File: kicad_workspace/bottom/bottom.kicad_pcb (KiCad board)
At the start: 2 copper layers, 76.8 x 84 mm, 12 parts, among them M1 N20_MOTOR_EXTENDED_SHAFT, M2 N20_MOTOR_EXTENDED_SHAFT, U1 DRV8833PWP, U2 ULTRASOUND_T_R, U3 ATmega4809-A, U4 BNO055, Y1 32.768kHz

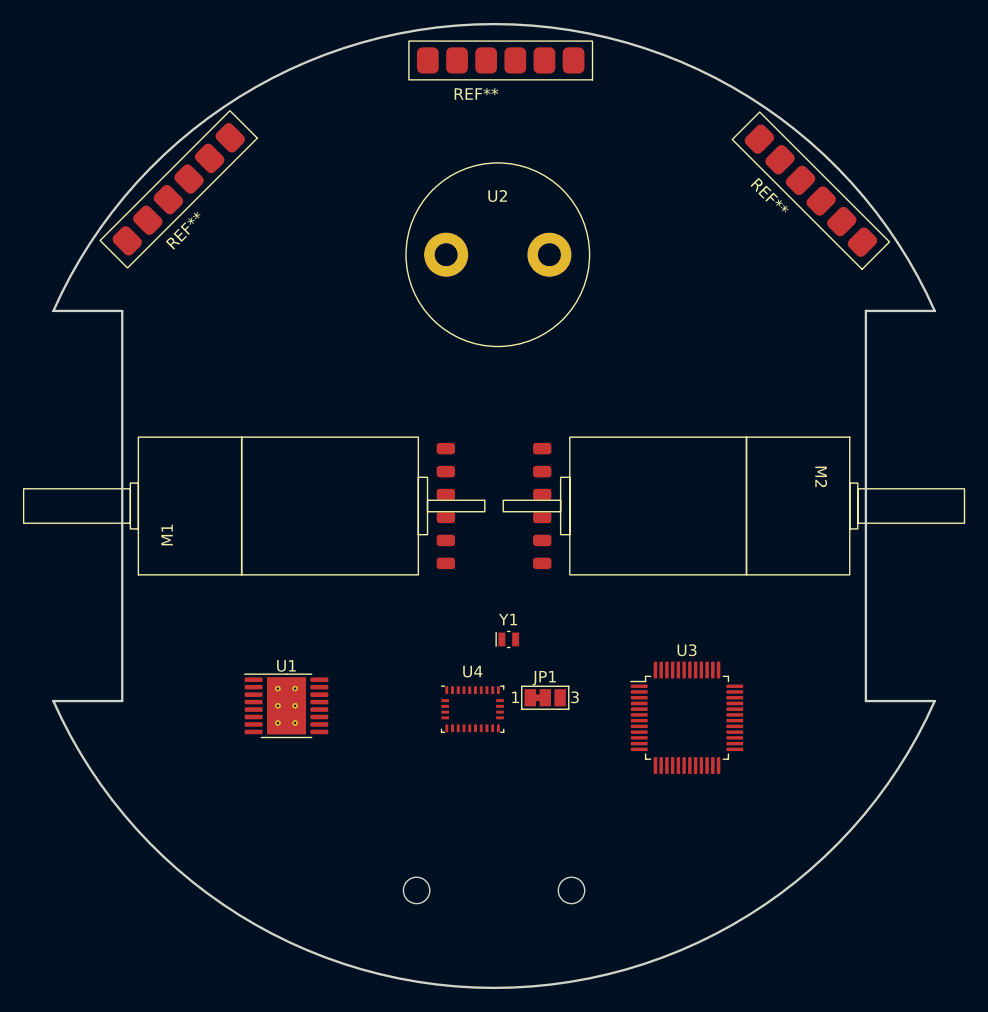
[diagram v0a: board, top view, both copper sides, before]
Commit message: add vl53l0x to schematic, connect footprint to sensors symbol
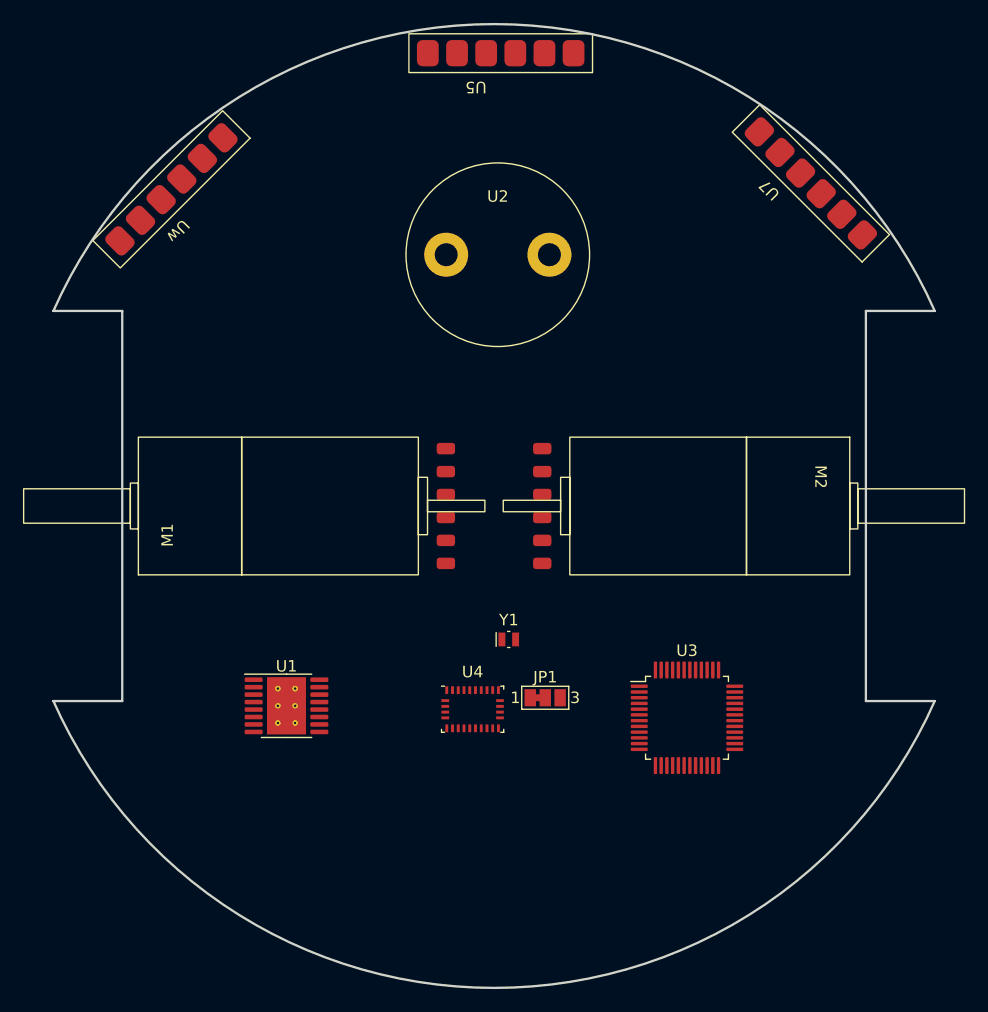
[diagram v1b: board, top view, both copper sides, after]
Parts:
- removed REF** (x3): VL53L0X, pololu:VL53L0X
- removed REF**: BALL_CASTER_3_8, pololu:BALL_CASTER_3_8
- added U5: ~, pololu:VL53L0X, F.Cu at (68.6, 22.2)
- added U7: ~, pololu:VL53L0X, F.Cu at (92.1, 38.7)
- added Uw: ~, pololu:VL53L0X, F.Cu at (38.7, 27.9)
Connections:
- net BNO_SCL renamed SCL
- net BNO_SDA renamed SDA
- U3 pad 10: unconnected-(U3-PC0-Pad10) -> VL_EN1
- U3 pad 11: unconnected-(U3-PC1-Pad11) -> VL_EN2
- U3 pad 12: unconnected-(U3-PC2-Pad12) -> VL_EN3

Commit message: change vcc and vdd symbols. add routes for bno055 sensor on pcb
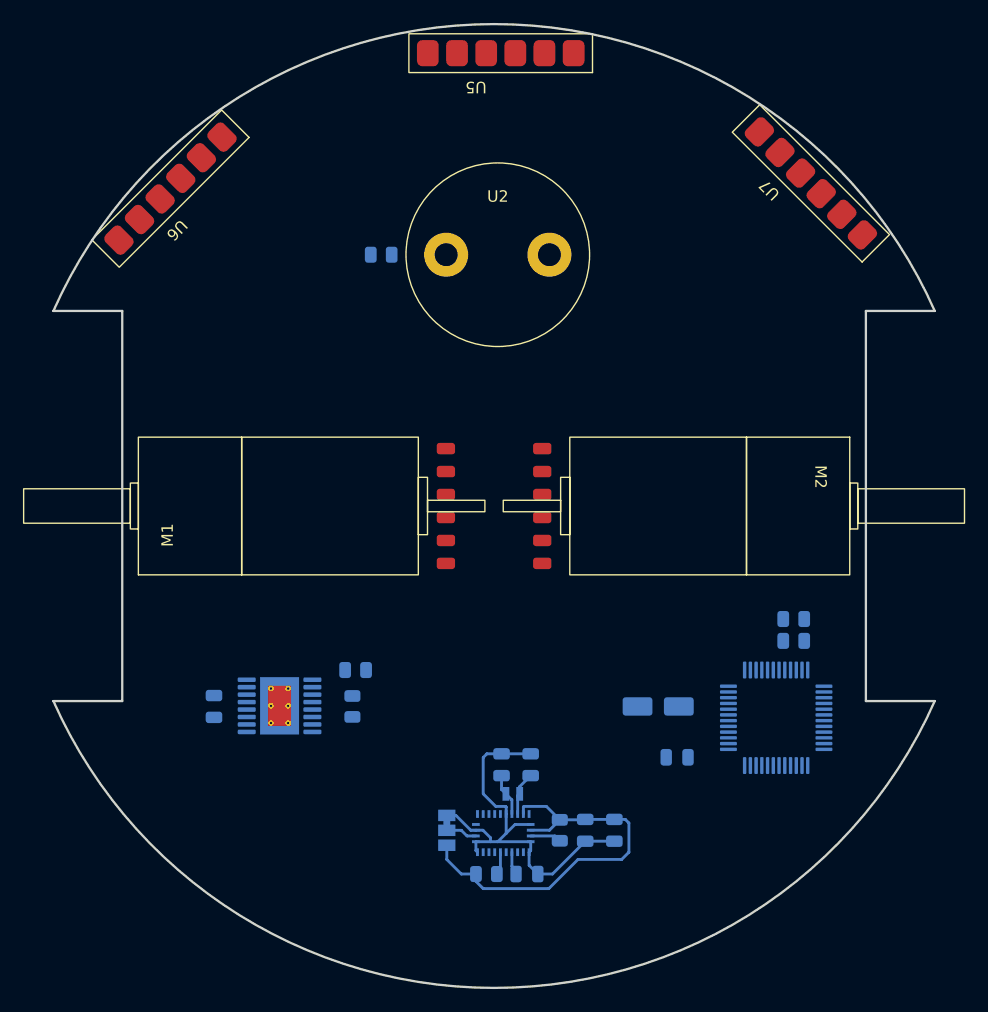
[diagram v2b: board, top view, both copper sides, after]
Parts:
- removed Uw: ~, pololu:VL53L0X
- added C1: 10nF, Capacitor_SMD:C_0805_2012Metric, B.Cu at (35.6, 77.5)
- added C2: 100nF, Capacitor_SMD:C_0805_2012Metric, B.Cu at (76.0, 81.9)
- added C3: 10uF, Capacitor_SMD:CP_Elec_4x3, B.Cu at (74.3, 77.5)
- added C4: 1uF, Capacitor_SMD:C_0805_2012Metric, B.Cu at (62.9, 92.1)
- added C5: 100nF, Capacitor_SMD:C_0805_2012Metric, B.Cu at (70.5, 88.3)
- added C6: 22pF, Capacitor_SMD:C_0805_2012Metric, B.Cu at (60.6, 82.5)
- added C7: 22pF, Capacitor_SMD:C_0805_2012Metric, B.Cu at (63.2, 82.5)
- added C8: 120nF, Capacitor_SMD:C_0805_2012Metric, B.Cu at (67.9, 88.3)
- added R1: 0.2R, Resistor_SMD:R_0805_2012Metric, B.Cu at (47.9, 74.3)
- added R2: 0.2R, Resistor_SMD:R_0805_2012Metric, B.Cu at (47.7, 77.5)
- added R3: R, Resistor_SMD:R_0805_2012Metric, B.Cu at (50.2, 38.1)
- added R4: 10K, Resistor_SMD:R_0805_2012Metric, B.Cu at (59.3, 92.1)
- added R5: 10K, Resistor_SMD:R_0805_2012Metric, B.Cu at (65.7, 88.3)
- added R6: R, Resistor_SMD:R_0805_2012Metric, B.Cu at (86.1, 69.8)
- added R7: R, Resistor_SMD:R_0805_2012Metric, B.Cu at (86.1, 71.8)
- added U6: ~, pololu:VL53L0X, F.Cu at (38.6, 27.9)
- JP1, U1, U3, U4, Y1: moved to B.Cu
- moved JP1 14.4 mm to (55.9, 88.3), turned to -90 degrees
- moved Y1 13.5 mm to (61.6, 85.1), turned to 180 degrees
- moved U4 11.1 mm to (60.8, 88.5), turned to 180 degrees
- moved U3 7.77 mm to (84.6, 78.5), turned to 180 degrees
- moved U1 0.60 mm to (41.3, 77.4), turned to 180 degrees
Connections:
- JP1 pad 3: VDD -> +3.3V
- M1 pad 4: VCC -> +3.3V
- M2 pad 4: VCC -> +3.3V
- U1 pad 12: VCC -> +5V
- U1 pad 14: VCC -> +3.3V
- U3 pad 14: VCC -> +3.3V
- U3 pad 28: VCC -> +3.3V
- U3 pad 42: VCC -> +3.3V
- U4 pad 28: VDD -> +3.3V
- U4 pad 3: VDD -> +3.3V
- U5 pad 1: VCC -> +3.3V
- U7 pad 1: VCC -> +3.3V
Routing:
- net GND: track 0.00 -> 37.9 mm
- net +3.3V: track 0.00 -> 35.8 mm
- net Net-(U4-XIN32): track 0.00 -> 3.82 mm
- net Net-(U4-XOUT32): track 0.00 -> 3.72 mm
- net Net-(JP1-C): track 0.00 -> 2.74 mm
- net Net-(U4-~{BOOT_LOAD_PIN}): track 0.00 -> 2.71 mm
- net Net-(U4-CAP): track 0.00 -> 2.50 mm
- net Net-(U4-~{RESET}): track 0.00 -> 2.03 mm

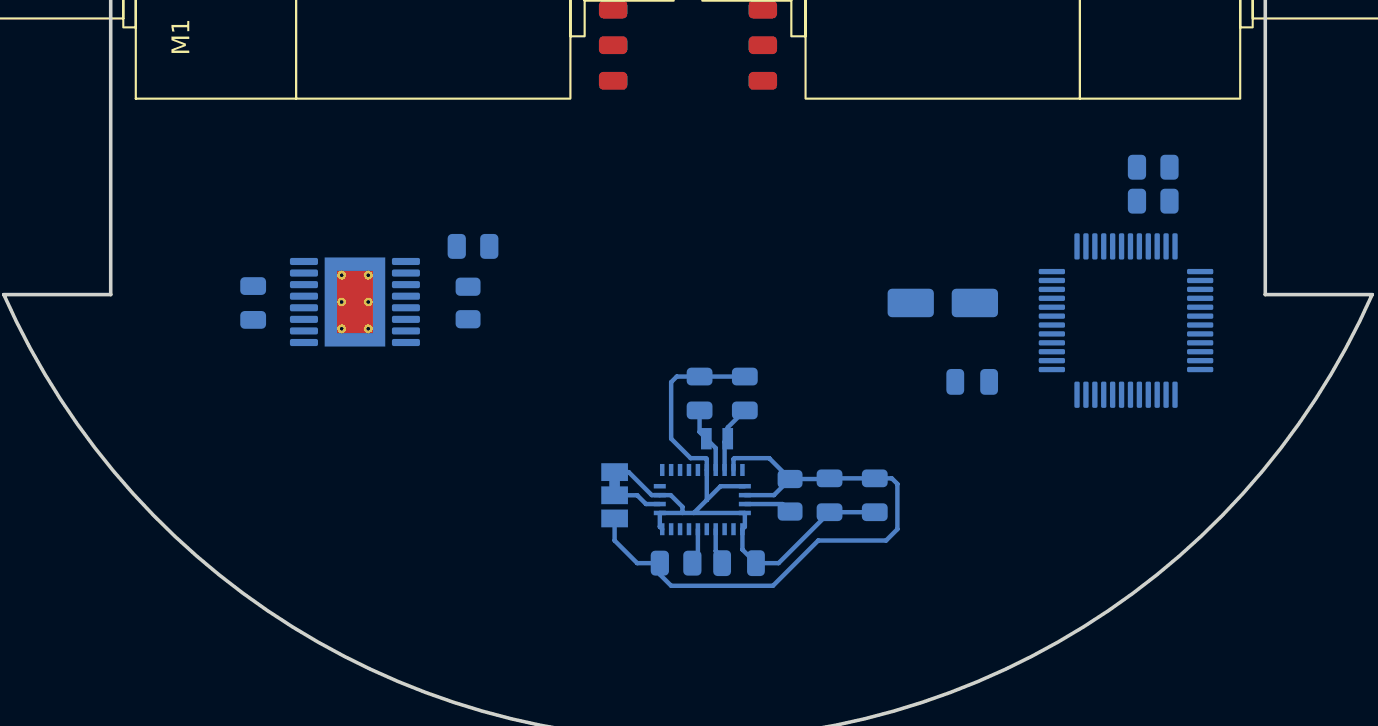
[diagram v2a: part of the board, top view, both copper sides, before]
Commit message: add 18650 samsung li ion battery to 3d preview
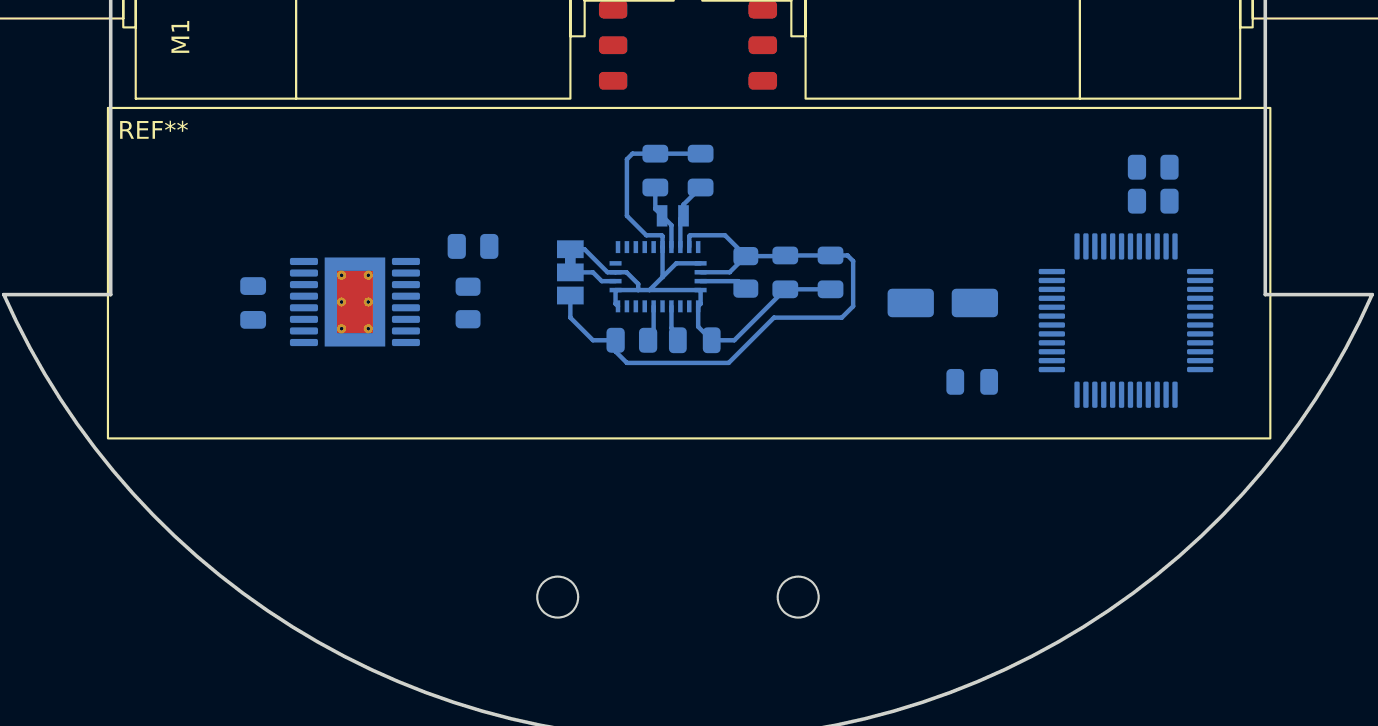
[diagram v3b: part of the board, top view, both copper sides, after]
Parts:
- added REF**: SAMSUNG_18650, pololu:SAMSUNG_18650, F.Cu at (27.4, 66.5)
- added REF**: BALL_CASTER_3_8, pololu:BALL_CASTER_3_8, B.Cu at (59.4, 94.0)
- moved C4 12.8 mm to (60.4, 79.6)
- moved C5 12.8 mm to (68.0, 75.8)
- moved C6 12.8 mm to (58.2, 70.0)
- moved C7 12.8 mm to (60.7, 70.0)
- moved C8 12.8 mm to (65.5, 75.8)
- moved JP1 12.8 mm to (53.4, 75.8)
- moved R4 12.8 mm to (56.8, 79.6)
- moved R5 12.8 mm to (63.2, 75.8)
- moved Y1 12.8 mm to (59.1, 72.6)
- moved U4 12.8 mm to (58.3, 76.0)
